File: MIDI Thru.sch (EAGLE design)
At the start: 49 parts, among them IC1 3N136, IC2 3N136, IC3 3N136, IC5 74HCT14, T1 2N3904, U1 7805T

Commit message: updating schematic
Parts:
- IC1, IC2, IC3: value 3N136 -> 6N136
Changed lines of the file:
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@@
 <part name="FRAME1" library="frames" library_urn="urn:adsk.eagle:library:229" deviceset="A4L-LOC" device=""/>
 <part name="D1" library="adafruit" library_urn="urn:adsk.eagle:library:420" deviceset="DIODE" device="DO-1N4148" value="1N4148"/>
-<part name="IC1" library="ic-package" library_urn="urn:adsk.eagle:library:239" deviceset="DIL8" device="" value="3N136"/>
+<part name="IC1" library="ic-package" library_urn="urn:adsk.eagle:library:239" deviceset="DIL8" device="" value="6N136"/>
 <part name="R1" library="eagle-ltspice" library_urn="urn:adsk.eagle:library:217" deviceset="R" device="0204/7" value="220"/>
 <part name="JP5" library="pinhead" library_urn="urn:adsk.eagle:library:325" deviceset="PINHD-1X2" device="" value="MIDI IN 2"/>
 <part name="D2" library="adafruit" library_urn="urn:adsk.eagle:library:420" deviceset="DIODE" device="DO-1N4148" value="1N4148"/>
-<part name="IC2" library="ic-package" library_urn="urn:adsk.eagle:library:239" deviceset="DIL8" device="" value="3N136"/>
+<part name="IC2" library="ic-package" library_urn="urn:adsk.eagle:library:239" deviceset="DIL8" device="" value="6N136"/>
 <part name="R2" library="eagle-ltspice" library_urn="urn:adsk.eagle:library:217" deviceset="R" device="0204/7" value="220"/>
 <part name="JP11" library="pinhead" library_urn="urn:adsk.eagle:library:325" deviceset="PINHD-1X2" device="" value="MIDI IN 3"/>
 <part name="D3" library="adafruit" library_urn="urn:adsk.eagle:library:420" deviceset="DIODE" device="DO-1N4148" value="1N4148"/>
-<part name="IC3" library="ic-package" library_urn="urn:adsk.eagle:library:239" deviceset="DIL8" device="" value="3N136"/>
+<part name="IC3" library="ic-package" library_urn="urn:adsk.eagle:library:239" deviceset="DIL8" device="" value="6N136"/>
 <part name="R3" library="eagle-ltspice" library_urn="urn:adsk.eagle:library:217" deviceset="R" device="0204/7" value="220"/>
 <part name="TEENSY_LC" library="Teensy_3_and_LC_Series_Boards_v1.4" deviceset="TEENSY_LC_ALL_PINS" device=""/>

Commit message: updating schematic
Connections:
- new net N$12: D3.C, IC3.2, R3.2
- new net N$7: JP4.1, R1.1
- new net N$9: D2.C, IC2.2, R2.2
- net N$1: no longer JP4.1, R1.1
- net N$3: no longer D2.C, IC2.2, R2.2
- net N$5: no longer D3.C, IC3.2, R3.2
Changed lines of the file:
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@@
 <net name="N$1" class="0">
 <segment>
-<pinref part="JP4" gate="G$1" pin="1"/>
-<wire x1="-73.66" y1="114.3" x2="-48.26" y2="114.3" width="0.1524" layer="91"/>
 <pinref part="IC1" gate="G$1" pin="2"/>
 <pinref part="D1" gate="G$1" pin="C"/>
-<wire x1="-48.26" y1="114.3" x2="-38.1" y2="114.3" width="0.1524" layer="91"/>
 <wire x1="-38.1" y1="114.3" x2="-35.56" y2="114.3" width="0.1524" layer="91"/>
 <wire x1="-35.56" y1="114.3" x2="-22.86" y2="114.3" width="0.1524" layer="91"/>
 <wire x1="-35.56" y1="111.76" x2="-35.56" y2="114.3" width="0.1524" layer="91"/>
 <junction x="-35.56" y="114.3"/>
-<pinref part="R1" gate="G$1" pin="1"/>
-<junction x="-48.26" y="114.3"/>
 <pinref part="R1" gate="G$1" pin="2"/>
-<junction x="-38.1" y="114.3"/>
 </segment>
 </net>
@@
 <pinref part="JP5" gate="G$1" pin="1"/>
 <wire x1="-73.66" y1="93.98" x2="-48.26" y2="93.98" width="0.1524" layer="91"/>
-<pinref part="IC2" gate="G$1" pin="2"/>
-<pinref part="D2" gate="G$1" pin="C"/>
-<wire x1="-48.26" y1="93.98" x2="-38.1" y2="93.98" width="0.1524" layer="91"/>
-<wire x1="-38.1" y1="93.98" x2="-35.56" y2="93.98" width="0.1524" layer="91"/>
-<wire x1="-35.56" y1="93.98" x2="-22.86" y2="93.98" width="0.1524" layer="91"/>
-<wire x1="-35.56" y1="91.44" x2="-35.56" y2="93.98" width="0.1524" layer="91"/>
-<junction x="-35.56" y="93.98"/>
 <pinref part="R2" gate="G$1" pin="1"/>
-<junction x="-48.26" y="93.98"/>
-<pinref part="R2" gate="G$1" pin="2"/>
-<junction x="-38.1" y="93.98"/>
 </segment>
 </net>
@@
 <pinref part="JP11" gate="G$1" pin="1"/>
 <wire x1="-73.66" y1="73.66" x2="-48.26" y2="73.66" width="0.1524" layer="91"/>
-<pinref part="IC3" gate="G$1" pin="2"/>
-<pinref part="D3" gate="G$1" pin="C"/>
-<wire x1="-48.26" y1="73.66" x2="-38.1" y2="73.66" width="0.1524" layer="91"/>
-<wire x1="-38.1" y1="73.66" x2="-35.56" y2="73.66" width="0.1524" layer="91"/>
-<wire x1="-35.56" y1="73.66" x2="-22.86" y2="73.66" width="0.1524" layer="91"/>
-<wire x1="-35.56" y1="71.12" x2="-35.56" y2="73.66" width="0.1524" layer="91"/>
-<junction x="-35.56" y="73.66"/>
 <pinref part="R3" gate="G$1" pin="1"/>
-<junction x="-48.26" y="73.66"/>
-<pinref part="R3" gate="G$1" pin="2"/>
-<junction x="-38.1" y="73.66"/>
 </segment>
 </net>
@@
 </segment>
 </net>
+<net name="N$7" class="0">
+<segment>
+<pinref part="R1" gate="G$1" pin="1"/>
+<pinref part="JP4" gate="G$1" pin="1"/>
+<wire x1="-48.26" y1="114.3" x2="-73.66" y2="114.3" width="0.1524" layer="91"/>
+</segment>
+</net>
+<net name="N$9" class="0">
+<segment>
+<pinref part="IC2" gate="G$1" pin="2"/>
+<wire x1="-35.56" y1="93.98" x2="-22.86" y2="93.98" width="0.1524" layer="91"/>
+<pinref part="D2" gate="G$1" pin="C"/>
+<wire x1="-35.56" y1="91.44" x2="-35.56" y2="93.98" width="0.1524" layer="91"/>
+<junction x="-35.56" y="93.98"/>
+<wire x1="-38.1" y1="93.98" x2="-35.56" y2="93.98" width="0.1524" layer="91"/>
+<pinref part="R2" gate="G$1" pin="2"/>
+</segment>
+</net>
+<net name="N$12" class="0">
+<segment>
+<pinref part="IC3" gate="G$1" pin="2"/>
+<wire x1="-35.56" y1="73.66" x2="-22.86" y2="73.66" width="0.1524" layer="91"/>
+<pinref part="D3" gate="G$1" pin="C"/>
+<wire x1="-35.56" y1="71.12" x2="-35.56" y2="73.66" width="0.1524" layer="91"/>
+<junction x="-35.56" y="73.66"/>
+<wire x1="-38.1" y1="73.66" x2="-35.56" y2="73.66" width="0.1524" layer="91"/>
+<pinref part="R3" gate="G$1" pin="2"/>
+</segment>
+</net>

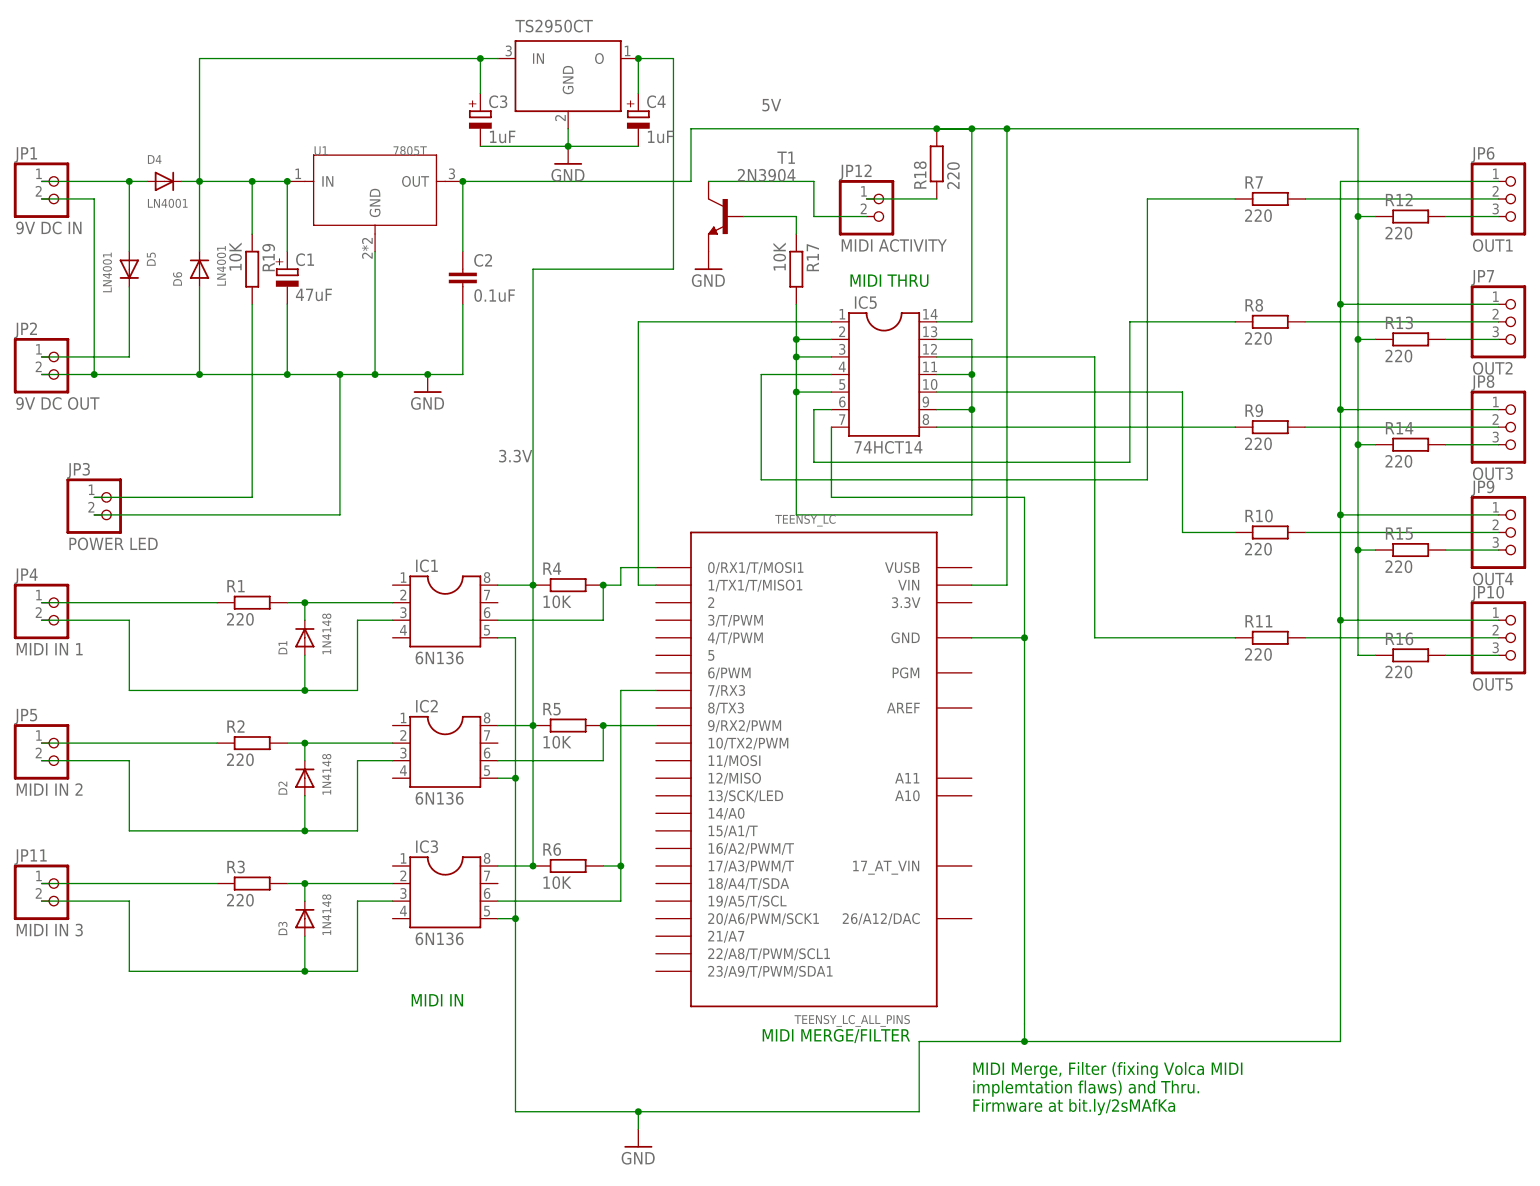
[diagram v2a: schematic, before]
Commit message: aligning component numbers with original to at least try to make veroboarding easier
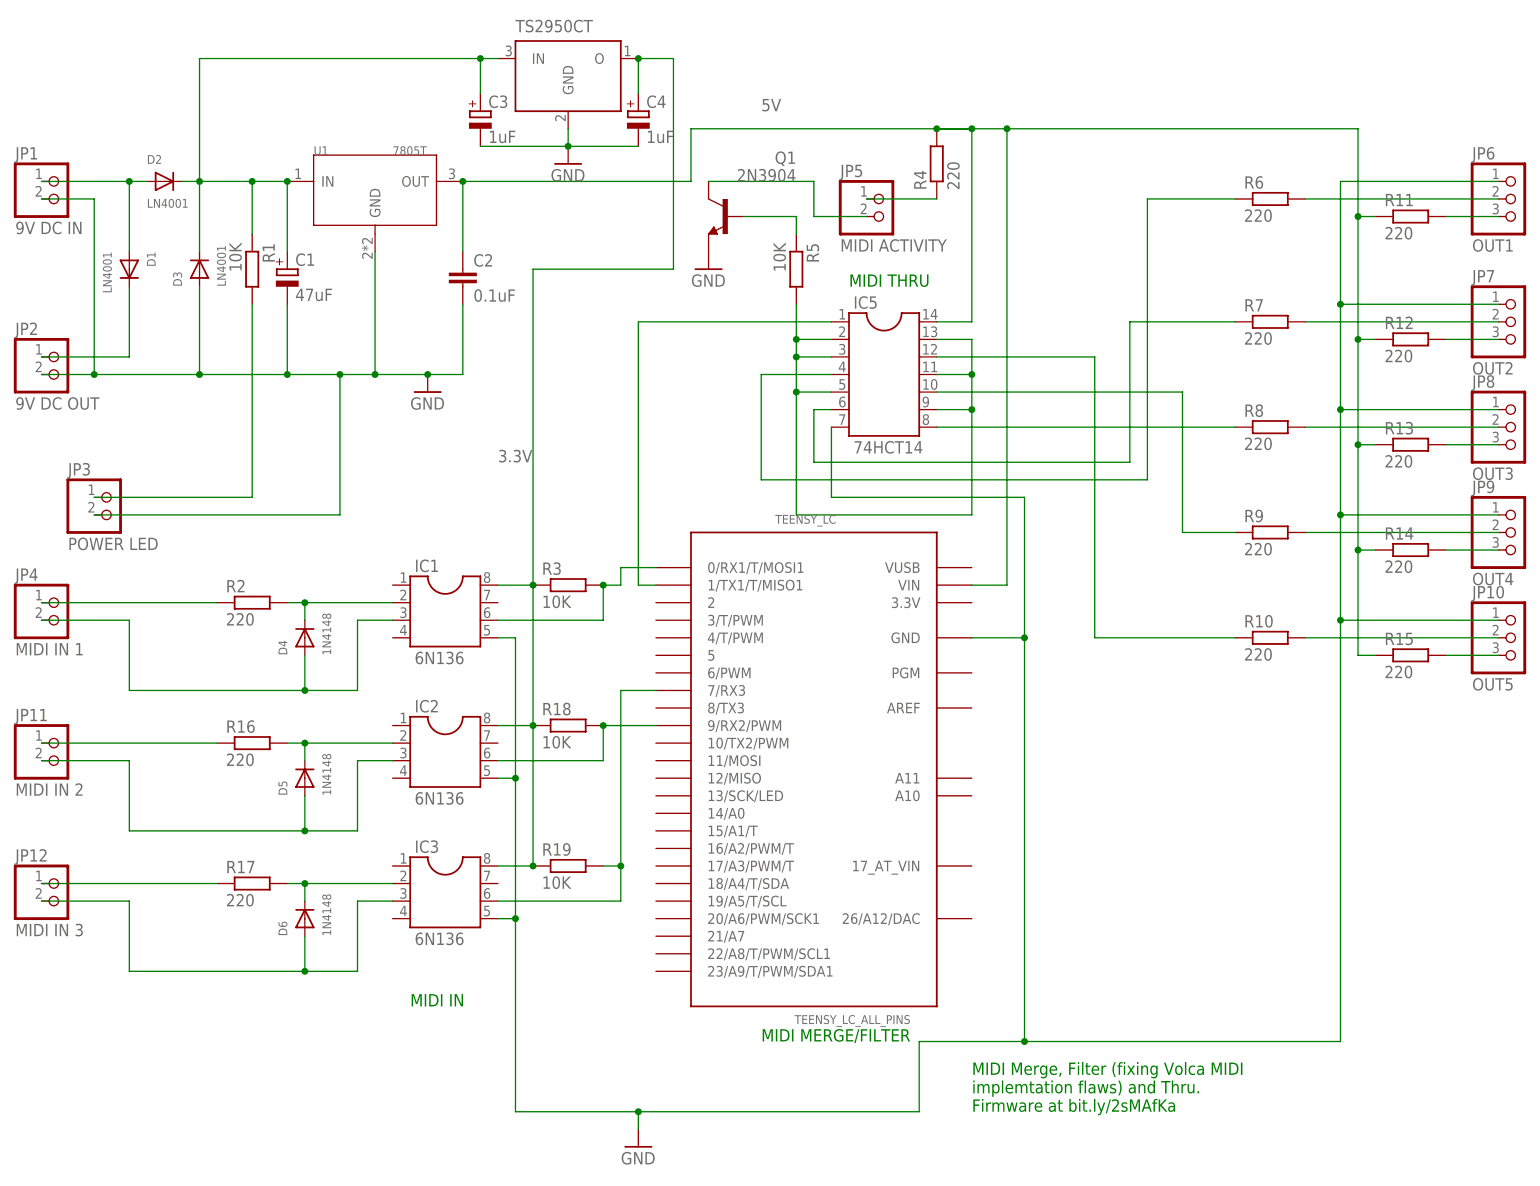
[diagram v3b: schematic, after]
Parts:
- D1, D2, D3: value 1N4148 -> LN4001
- D4, D5, D6: value LN4001 -> 1N4148
- JP11: value MIDI IN 3 -> MIDI IN 2
- JP12: value MIDI ACTIVITY -> MIDI IN 3
- JP5: value MIDI IN 2 -> MIDI ACTIVITY
- R1, R18, R3: value 220 -> 10K
- R17, R4, R6: value 10K -> 220
- renumbered T1 to Q1
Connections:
- net 3.3V: now also R18.1, R19.1, R3.1; no longer R4.1, R5.1, R6.1
- net 5V: now also R11.1, R4.2; no longer R16.1, R18.2
- net GND: now also D3.A; no longer D6.A
- net N$1: now also D4.C, R2.2; no longer D1.C, R1.2
- net N$10: now also R18.2; no longer R5.2
- net N$11: now also R19.2; no longer R6.2
- net N$12: now also D6.C, R17.2; no longer D3.C, R3.2
- net N$14: now also R6.1; no longer R7.1
- net N$15: now also R6.2; no longer R7.2
- net N$17: now also R11.2; no longer R12.2
- net N$18: now also R12.2; no longer R13.2
- net N$19: now also R13.2; no longer R14.2
- net N$2: now also D4.A; no longer D1.A
- net N$20: now also R14.2; no longer R15.2
- net N$21: now also R15.2; no longer R16.2
- net N$23: now also R7.1; no longer R8.1
- net N$24: now also R7.2; no longer R8.2
- net N$25: now also R5.1; no longer R17.1
- net N$26: now also R8.1; no longer R9.1
- net N$27: now also R8.2; no longer R9.2
- net N$28: now also R9.1; no longer R10.1
- net N$29: now also R9.2; no longer R10.2
- net N$3: now also JP11.1, R16.1; no longer JP5.1, R2.1
- net N$30: now also R10.1; no longer R11.1
- net N$31: now also R10.2; no longer R11.2
- net N$32: now also JP5.2; no longer JP12.2
- net N$33: now also R5.2; no longer R17.2
- net N$34: now also JP5.1, R4.1; no longer JP12.1, R18.1
- net N$35: now also D1.A, D2.A; no longer D4.A, D5.A
- net N$36: now also D1.C; no longer D5.C
- net N$38: now also D2.C, D3.C, R1.1; no longer D4.C, D6.C, R19.1
- net N$39: now also R1.2; no longer R19.2
- net N$4: now also D5.A, JP11.2; no longer D2.A, JP5.2
- net N$5: now also JP12.1, R17.1; no longer JP11.1, R3.1
- net N$6: now also D6.A, JP12.2; no longer D3.A, JP11.2
- net N$7: now also R2.1; no longer R1.1
- net N$8: now also R3.2; no longer R4.2
- net N$9: now also D5.C, R16.2; no longer D2.C, R2.2
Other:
- moved on the sheet: D1, D2, D3, D4, D5, D6, JP11, JP12, JP5, R1, R10, R11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
